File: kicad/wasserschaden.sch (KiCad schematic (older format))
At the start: 13 parts, among them J1 valve out, J2 12V in, U1 stepdown, U2 WeMos_mini

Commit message: added deepsleep jumper to schematic &cleanup
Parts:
- added JP?: SolderJumper_2_Open, symbol Jumper:SolderJumper_2_Open
- D1: symbol wasserschaden-rescue:D -> wasserschaden-cache-2018-10-17-20-35-24:D
- D2, D3, D4: symbol wasserschaden-rescue:LED -> wasserschaden-cache-2018-10-17-20-35-24:LED
- IRFZ44N1: symbol wasserschaden-rescue:2N7000 -> wasserschaden-cache-2018-10-17-20-35-24:2N7000
- J1, J2: symbol wasserschaden-rescue:Screw_Terminal_01x02 -> wasserschaden-cache-2018-10-17-20-35-24:Screw_Terminal_01x02
- R1, R2, R3, R4: symbol wasserschaden-rescue:R -> wasserschaden-cache-2018-10-17-20-35-24:R
- U1: symbol wasserschaden-rescue:stepdown -> wasserschaden-cache-2018-10-17-20-35-24:stepdown
- U2: symbol wasserschaden-rescue:WeMos_mini -> wasserschaden-cache-2018-10-17-20-35-24:WeMos_mini
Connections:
- wire segments 16 -> 21
- no-connect marks 12 -> 10
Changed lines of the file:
@@
 EESchema Schematic File Version 4
-LIBS:wasserschaden-cache
 EELAYER 26 0
 EELAYER END
@@
 $EndDescr
 $Comp
-L wasserschaden-rescue:WeMos_mini U2
+L wasserschaden-cache-2018-10-17-20-35-24:WeMos_mini U2
 U 1 1 5B26FC39
 P 4000 2100
@@
 $EndComp
 $Comp
-L wasserschaden-rescue:2N7000 IRFZ44N1
+L wasserschaden-cache-2018-10-17-20-35-24:2N7000 IRFZ44N1
 U 1 1 5B2A69C6
 P 2900 2250
@@
 	3100 2250 3200 2250
 $Comp
-L wasserschaden-rescue:Screw_Terminal_01x02 J1
+L wasserschaden-cache-2018-10-17-20-35-24:Screw_Terminal_01x02 J1
 U 1 1 5B2A6B15
 P 2450 2750
@@
 $EndComp
 $Comp
-L wasserschaden-rescue:Screw_Terminal_01x02 J2
+L wasserschaden-cache-2018-10-17-20-35-24:Screw_Terminal_01x02 J2
 U 1 1 5B2A6B9D
 P 2450 3200
@@
 $EndComp
 $Comp
-L wasserschaden-rescue:GND #PWR01
+L wasserschaden-cache-2018-10-17-20-35-24:GND #PWR01
 U 1 1 5B2A6BE6
 P 2650 3200
@@
 $EndComp
 $Comp
-L wasserschaden-rescue:GND #PWR02
+L wasserschaden-cache-2018-10-17-20-35-24:GND #PWR02
 U 1 1 5B2A6C2A
 P 3500 1850
@@
 $EndComp
 $Comp
-L wasserschaden-rescue:GND #PWR03
+L wasserschaden-cache-2018-10-17-20-35-24:GND #PWR03
 U 1 1 5B2A6C5A
 P 2800 2050
@@
 $EndComp
 $Comp
-L wasserschaden-rescue:D D1
+L wasserschaden-cache-2018-10-17-20-35-24:D D1
 U 1 1 5B2A6D63
 P 3050 2750
@@
 $EndComp
 $Comp
-L wasserschaden-rescue:stepdown U1
+L wasserschaden-cache-2018-10-17-20-35-24:stepdown U1
 U 1 1 5B2A6F8D
 P 3800 3000
@@
 	4500 1750 4950 1750
 $Comp
-L wasserschaden-rescue:GND #PWR04
+L wasserschaden-cache-2018-10-17-20-35-24:GND #PWR04
 U 1 1 5B2A7077
 P 3400 2900
@@
 NoConn ~ 3500 2350
 NoConn ~ 3500 2450
-NoConn ~ 4500 2450
 NoConn ~ 4500 2350
-NoConn ~ 4500 2250
 NoConn ~ 4500 2150
 NoConn ~ 4500 2050
@@
 +\n-
 Wire Wire Line
-	4950 1750 4950 2000
-Wire Wire Line
 	2650 2650 3200 2650
 Wire Wire Line
 	3200 2650 3200 2750
 $Comp
-L wasserschaden-rescue:+12V #PWR05
+L wasserschaden-cache-2018-10-17-20-35-24:+12V #PWR05
 U 1 1 5B2A7A00
 P 2650 2650
@@
 $EndComp
 $Comp
-L wasserschaden-rescue:+12V #PWR06
+L wasserschaden-cache-2018-10-17-20-35-24:+12V #PWR06
 U 1 1 5B2A7A20
 P 2650 3100
@@
 $EndComp
 $Comp
-L wasserschaden-rescue:+12V #PWR07
+L wasserschaden-cache-2018-10-17-20-35-24:+12V #PWR07
 U 1 1 5B2A7A40
 P 3400 3050
@@
 $EndComp
 $Comp
-L wasserschaden-rescue:R R1
+L wasserschaden-cache-2018-10-17-20-35-24:R R1
 U 1 1 5B2A7CB0
 P 3050 2100
@@
 $EndComp
 $Comp
-L wasserschaden-rescue:GND #PWR08
+L wasserschaden-cache-2018-10-17-20-35-24:GND #PWR08
 U 1 1 5B2A7CE4
 P 3050 1950
@@
 $EndComp
 $Comp
-L wasserschaden-rescue:GND #PWR09
+L wasserschaden-cache-2018-10-17-20-35-24:GND #PWR09
 U 1 1 5B2A9F12
 P 4700 2900
@@
 	4950 3050 4700 3050
 $Comp
-L wasserschaden-rescue:LED D2
+L wasserschaden-cache-2018-10-17-20-35-24:LED D2
 U 1 1 5B2BDC1C
 P 3200 1500
@@
 $EndComp
 $Comp
-L wasserschaden-rescue:R R2
+L wasserschaden-cache-2018-10-17-20-35-24:R R2
 U 1 1 5B2BDCBD
 P 3200 1200
@@
 $EndComp
 $Comp
-L wasserschaden-rescue:GND #PWR010
+L wasserschaden-cache-2018-10-17-20-35-24:GND #PWR010
 U 1 1 5B2BDCFD
 P 3200 1050
@@
 	-1   0    0    1
 $EndComp
-Connection ~ 4950 2000
 Wire Wire Line
 	3200 1650 3200 2250
 Connection ~ 3200 2250
 $Comp
-L wasserschaden-rescue:LED D3
+L wasserschaden-cache-2018-10-17-20-35-24:LED D3
 U 1 1 5B2C19FD
 P 5100 2000
@@
 $EndComp
 $Comp
-L wasserschaden-rescue:R R3
+L wasserschaden-cache-2018-10-17-20-35-24:R R3
 U 1 1 5B2C1A03
 P 5250 2150
@@
 $EndComp
 $Comp
-L wasserschaden-rescue:GND #PWR011
+L wasserschaden-cache-2018-10-17-20-35-24:GND #PWR011
 U 1 1 5B2C1A09
 P 5250 2300
@@
 $EndComp
 $Comp
-L wasserschaden-rescue:LED D4
+L wasserschaden-cache-2018-10-17-20-35-24:LED D4
 U 1 1 5B2C1D4C
 P 3450 1500
@@
 $EndComp
 $Comp
-L wasserschaden-rescue:R R4
+L wasserschaden-cache-2018-10-17-20-35-24:R R4
 U 1 1 5B2C1D52
 P 3450 1200
@@
 $EndComp
 $Comp
-L wasserschaden-rescue:GND #PWR012
+L wasserschaden-cache-2018-10-17-20-35-24:GND #PWR012
 U 1 1 5B2C1D58
 P 3450 1050
@@
 	3300 2150 3500 2150
 $Comp
-L wasserschaden-rescue:+3.3V #PWR013
+L wasserschaden-cache-2018-10-17-20-35-24:+3V3 #PWR013
 U 1 1 5B2C1F93
 P 4950 1750
@@
 	2800 2750 2900 2750
 Wire Wire Line
-	4950 2000 4950 3050
-Wire Wire Line
 	3200 2250 3500 2250
+Wire Wire Line
+	4950 1750 4950 3050
+$Comp
+L Jumper:SolderJumper_2_Open JP?
+U 1 1 5BCFAE3F
+P 4750 2350
+F 0 "JP?" V 4704 2418 50  0000 L CNN
+F 1 "SolderJumper_2_Open" V 4795 2418 50  0000 L CNN
+F 2 "" H 4750 2350 50  0001 C CNN
+F 3 "~" H 4750 2350 50  0001 C CNN
+	1    4750 2350
+	0    1    1    0
+$EndComp
+Wire Wire Line
+	4750 2200 4600 2200
+Wire Wire Line
+	4600 2200 4600 2250
+Wire Wire Line
+	4600 2250 4500 2250
+Wire Wire Line
+	4500 2450 4600 2450
+Wire Wire Line
+	4600 2450 4600 2500
+Wire Wire Line
+	4600 2500 4750 2500
 $EndSCHEMATC

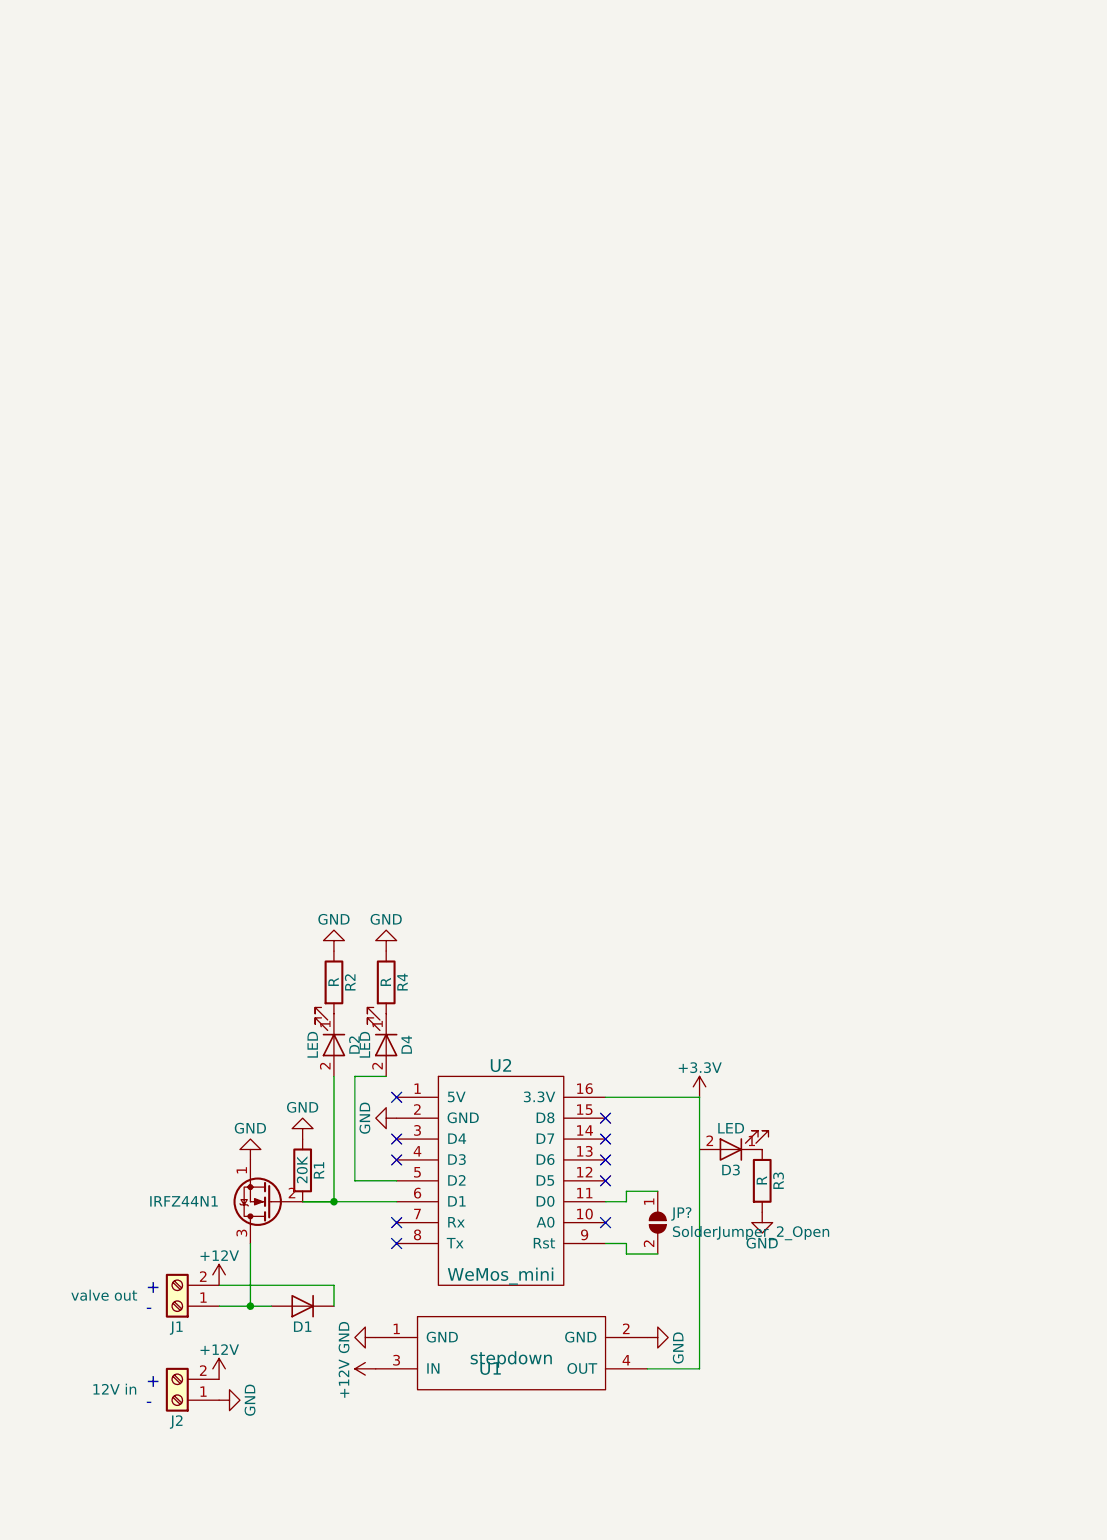
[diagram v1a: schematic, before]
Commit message: added jumper to pcb
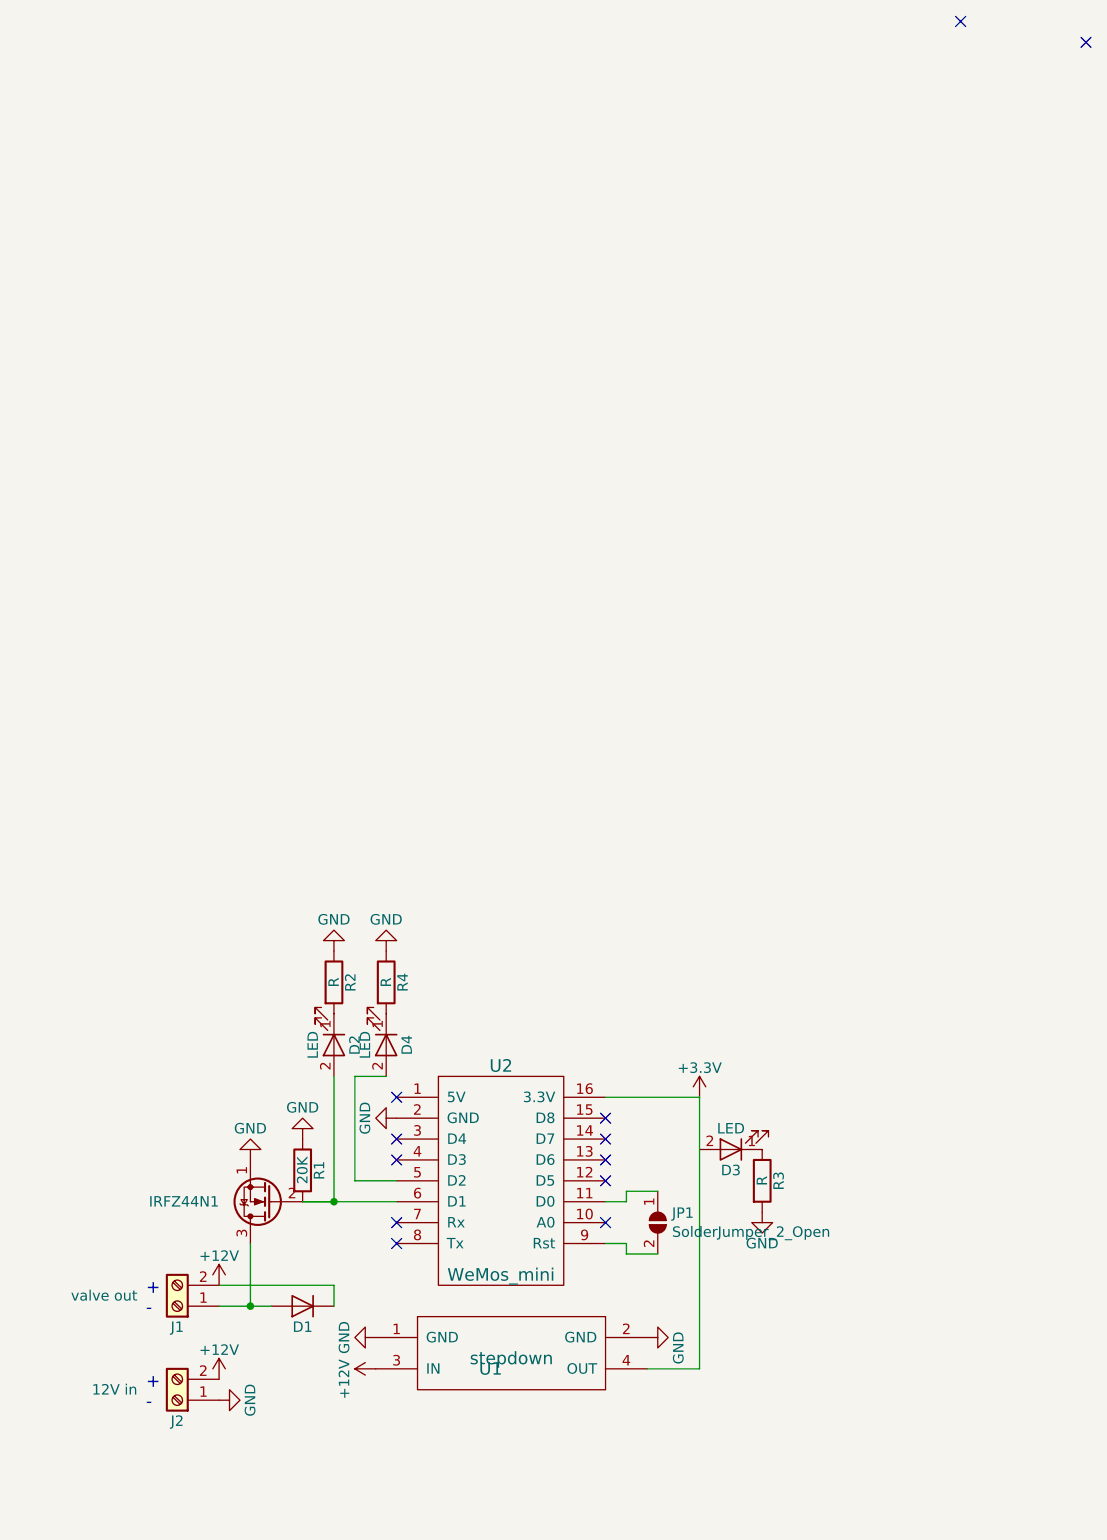
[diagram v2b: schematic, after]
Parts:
- IRFZ44N1: footprint test_wemos:irlz44n -> custom:irlz44n
- JP1: renamed from JP?; footprint (none) -> custom:jumper
- U1: footprint stepdown:stepdown -> custom:stepdown
- U2: footprint test_wemos:wemos-d1-mini-with-pin-header -> custom:wemos
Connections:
- no-connect marks 10 -> 12
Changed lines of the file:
@@
 EESchema Schematic File Version 4
+LIBS:wasserschaden-cache
 EELAYER 26 0
 EELAYER END
@@
 F 0 "U2" H 4000 2600 60  0000 C CNN
 F 1 "WeMos_mini" H 4000 1600 60  0000 C CNN
-F 2 "test_wemos:wemos-d1-mini-with-pin-header" H 4550 1400 60  0001 C CNN
+F 2 "custom:wemos" H 4550 1400 60  0001 C CNN
 F 3 "" H 4550 1400 60  0000 C CNN
 	1    4000 2100
@@
 F 0 "IRFZ44N1" H 3150 2250 50  0000 L CNN
 F 1 " " H 3100 2250 50  0000 L CNN
-F 2 "test_wemos:irlz44n" H 3100 2175 50  0001 L CIN
+F 2 "custom:irlz44n" H 3100 2175 50  0001 L CIN
 F 3 "" H 2900 2250 50  0001 L CNN
 	1    2900 2250
@@
 F 0 "U1" H 3950 2950 60  0000 C CNN
 F 1 "stepdown" H 4050 3000 60  0000 C CNN
-F 2 "stepdown:stepdown" H 3800 3000 60  0001 C CNN
+F 2 "custom:stepdown" H 3800 3000 60  0001 C CNN
 F 3 "" H 3800 3000 60  0001 C CNN
 	1    3800 3000
@@
 	4950 1750 4950 3050
 $Comp
-L Jumper:SolderJumper_2_Open JP?
+L Jumper:SolderJumper_2_Open JP1
 U 1 1 5BCFAE3F
 P 4750 2350
-F 0 "JP?" V 4704 2418 50  0000 L CNN
+F 0 "JP1" V 4704 2418 50  0000 L CNN
 F 1 "SolderJumper_2_Open" V 4795 2418 50  0000 L CNN
-F 2 "" H 4750 2350 50  0001 C CNN
+F 2 "custom:jumper" H 4750 2350 50  0001 C CNN
 F 3 "~" H 4750 2350 50  0001 C CNN
 	1    4750 2350
@@
 Wire Wire Line
 	4600 2500 4750 2500
+NoConn ~ 6200 -3400
+NoConn ~ 6800 -3300
 $EndSCHEMATC

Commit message: added sense jumper to schematic
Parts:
- added J3: sense, Connectors_Terminal_Blocks:TerminalBlock_Altech_AK300-2_P5.00mm, symbol wasserschaden-cache-2018-10-17-20-35-24:Screw_Terminal_01x02
- added JP2: sense jumper, symbol Device:Jumper_NC_Dual
- JP1: value SolderJumper_2_Open -> deepsleep jumper
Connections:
- wire segments 21 -> 29
- no-connect marks 12 -> 11
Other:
- moved on the sheet: D1, D2, D4, IRFZ44N1, J1, R1, R2, R4

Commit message: added sense input
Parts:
- removed JP2: sense jumper, symbol Device:Jumper_NC_Dual
- added R5: R, Resistors_THT:R_Axial_DIN0207_L6.3mm_D2.5mm_P7.62mm_Horizontal, symbol Device:R
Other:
- moved on the sheet: J3, R1
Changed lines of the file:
@@
 	-1   0    0    1
 $EndComp
-Wire Wire Line
-	2900 2250 3000 2250
 $Comp
 L wasserschaden-cache-2018-10-17-20-35-24:Screw_Terminal_01x02 J1
@@
 NoConn ~ 4500 1850
 Wire Wire Line
-	2650 2750 2700 2750
-Wire Wire Line
 	2600 2450 2600 2750
 Text Notes 2100 2800 0    60   ~ 0
@@
 L wasserschaden-cache-2018-10-17-20-35-24:R R1
 U 1 1 5B2A7CB0
-P 2850 2100
-F 0 "R1" V 2930 2100 50  0000 C CNN
-F 1 "20K" V 2850 2100 50  0000 C CNN
-F 2 "Resistors_THT:R_Axial_DIN0207_L6.3mm_D2.5mm_P7.62mm_Horizontal" V 2780 2100 50  0001 C CNN
-F 3 "" H 2850 2100 50  0001 C CNN
-	1    2850 2100
-	1    0    0    -1
+P 3000 2400
+F 0 "R1" V 3080 2400 50  0000 C CNN
+F 1 "20K" V 3000 2400 50  0000 C CNN
+F 2 "Resistors_THT:R_Axial_DIN0207_L6.3mm_D2.5mm_P7.62mm_Horizontal" V 2930 2400 50  0001 C CNN
+F 3 "" H 3000 2400 50  0001 C CNN
+	1    3000 2400
+	-1   0    0    1
 $EndComp
 $Comp
 L wasserschaden-cache-2018-10-17-20-35-24:GND #PWR08
 U 1 1 5B2A7CE4
-P 2850 1950
-F 0 "#PWR08" H 2850 1700 50  0001 C CNN
-F 1 "GND" H 2850 1800 50  0000 C CNN
-F 2 "" H 2850 1950 50  0001 C CNN
-F 3 "" H 2850 1950 50  0001 C CNN
-	1    2850 1950
-	-1   0    0    1
+P 3000 2550
+F 0 "#PWR08" H 3000 2300 50  0001 C CNN
+F 1 "GND" H 3000 2400 50  0000 C CNN
+F 2 "" H 3000 2550 50  0001 C CNN
+F 3 "" H 3000 2550 50  0001 C CNN
+	1    3000 2550
+	0    -1   -1   0
 $EndComp
 $Comp
@@
 	-1   0    0    1
 $EndComp
-Wire Wire Line
-	3000 1650 3000 2250
 Connection ~ 3000 2250
 $Comp
@@
 	1    0    0    -1
 $EndComp
-Wire Wire Line
-	4950 1750 4950 3050
 $Comp
 L Jumper:SolderJumper_2_Open JP1
@@
 NoConn ~ 4500 2150
 Connection ~ 2450 2650
-Connection ~ 2700 2750
-Connection ~ 2900 2250
-Wire Wire Line
-	2900 2250 2850 2250
-Wire Wire Line
-	2700 2750 2900 2750
 Wire Wire Line
 	3100 2150 3500 2150
@@
 Wire Wire Line
 	3200 1700 3450 1700
-Wire Wire Line
-	3450 1700 3450 1200
 $Comp
 L wasserschaden-cache-2018-10-17-20-35-24:Screw_Terminal_01x02 J3
 U 1 1 5BE7342F
-P 3950 900
-F 0 "J3" H 3950 1000 50  0000 C CNN
-F 1 "sense" V 4050 900 50  0000 C CNN
-F 2 "Connectors_Terminal_Blocks:TerminalBlock_Altech_AK300-2_P5.00mm" H 3950 900 50  0001 C CNN
-F 3 "" H 3950 900 50  0001 C CNN
-	1    3950 900
-	0    -1   -1   0
-$EndComp
-$Comp
-L Device:Jumper_NC_Dual JP2
-U 1 1 5BE73632
-P 4400 1150
-F 0 "JP2" V 4354 1252 50  0000 L CNN
-F 1 "sense jumper" V 4445 1252 50  0000 L CNN
-F 2 "" H 4400 1150 50  0001 C CNN
-F 3 "~" H 4400 1150 50  0001 C CNN
-	1    4400 1150
-	0    1    1    0
-$EndComp
-Wire Wire Line
-	3450 1200 3950 1200
-Wire Wire Line
-	4050 1150 4300 1150
-$Comp
-L power:+3.3V #PWR0101
-U 1 1 5BE747AE
-P 4400 900
-F 0 "#PWR0101" H 4400 750 50  0001 C CNN
-F 1 "+3.3V" H 4415 1073 50  0000 C CNN
-F 2 "" H 4400 900 50  0001 C CNN
-F 3 "" H 4400 900 50  0001 C CNN
-	1    4400 900
-	1    0    0    -1
-$EndComp
+P 3950 800
+F 0 "J3" H 3950 900 50  0000 C CNN
+F 1 "sense" V 4050 800 50  0000 C CNN
+F 2 "Connectors_Terminal_Blocks:TerminalBlock_Altech_AK300-2_P5.00mm" H 3950 800 50  0001 C CNN
+F 3 "" H 3950 800 50  0001 C CNN
+	1    3950 800
+	0    -1   -1   0
+$EndComp
+Wire Wire Line
+	3450 1100 3950 1100
+Wire Wire Line
+	4050 1050 4300 1050
 $Comp
 L power:GND #PWR0102
 U 1 1 5BE7483F
-P 4400 1400
-F 0 "#PWR0102" H 4400 1150 50  0001 C CNN
-F 1 "GND" H 4405 1227 50  0000 C CNN
-F 2 "" H 4400 1400 50  0001 C CNN
-F 3 "" H 4400 1400 50  0001 C CNN
-	1    4400 1400
-	1    0    0    -1
-$EndComp
-Wire Wire Line
-	3950 1100 3950 1200
-Wire Wire Line
-	4050 1150 4050 1100
+P 4300 1050
+F 0 "#PWR0102" H 4300 800 50  0001 C CNN
+F 1 "GND" H 4305 877 50  0000 C CNN
+F 2 "" H 4300 1050 50  0001 C CNN
+F 3 "" H 4300 1050 50  0001 C CNN
+	1    4300 1050
+	1    0    0    -1
+$EndComp
+Wire Wire Line
+	3950 1000 3950 1100
+Wire Wire Line
+	4050 1050 4050 1000
+$Comp
+L Device:R R5
+U 1 1 5BE92986
+P 3950 1250
+F 0 "R5" H 4020 1296 50  0000 L CNN
+F 1 "R" H 4020 1205 50  0000 L CNN
+F 2 "Resistors_THT:R_Axial_DIN0207_L6.3mm_D2.5mm_P7.62mm_Horizontal" V 3880 1250 50  0001 C CNN
+F 3 "~" H 3950 1250 50  0001 C CNN
+	1    3950 1250
+	1    0    0    -1
+$EndComp
+Connection ~ 3950 1100
+Wire Wire Line
+	3450 1100 3450 1700
+$Comp
+L power:+3.3V #PWR0101
+U 1 1 5BE93467
+P 3950 1400
+F 0 "#PWR0101" H 3950 1250 50  0001 C CNN
+F 1 "+3.3V" V 3965 1528 50  0000 L CNN
+F 2 "" H 3950 1400 50  0001 C CNN
+F 3 "" H 3950 1400 50  0001 C CNN
+	1    3950 1400
+	0    -1   -1   0
+$EndComp
+Wire Wire Line
+	2450 2750 2600 2750
+Wire Wire Line
+	2700 2750 2600 2750
+Connection ~ 2600 2750
+Wire Wire Line
+	3000 1650 3000 2250
+Wire Wire Line
+	3000 2250 2900 2250
+Wire Wire Line
+	4950 1750 4950 2000
+Connection ~ 4950 2000
+Wire Wire Line
+	4950 2000 4950 3050
 $EndSCHEMATC
